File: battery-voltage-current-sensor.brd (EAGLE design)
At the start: 100 x 90 mm, 1 part

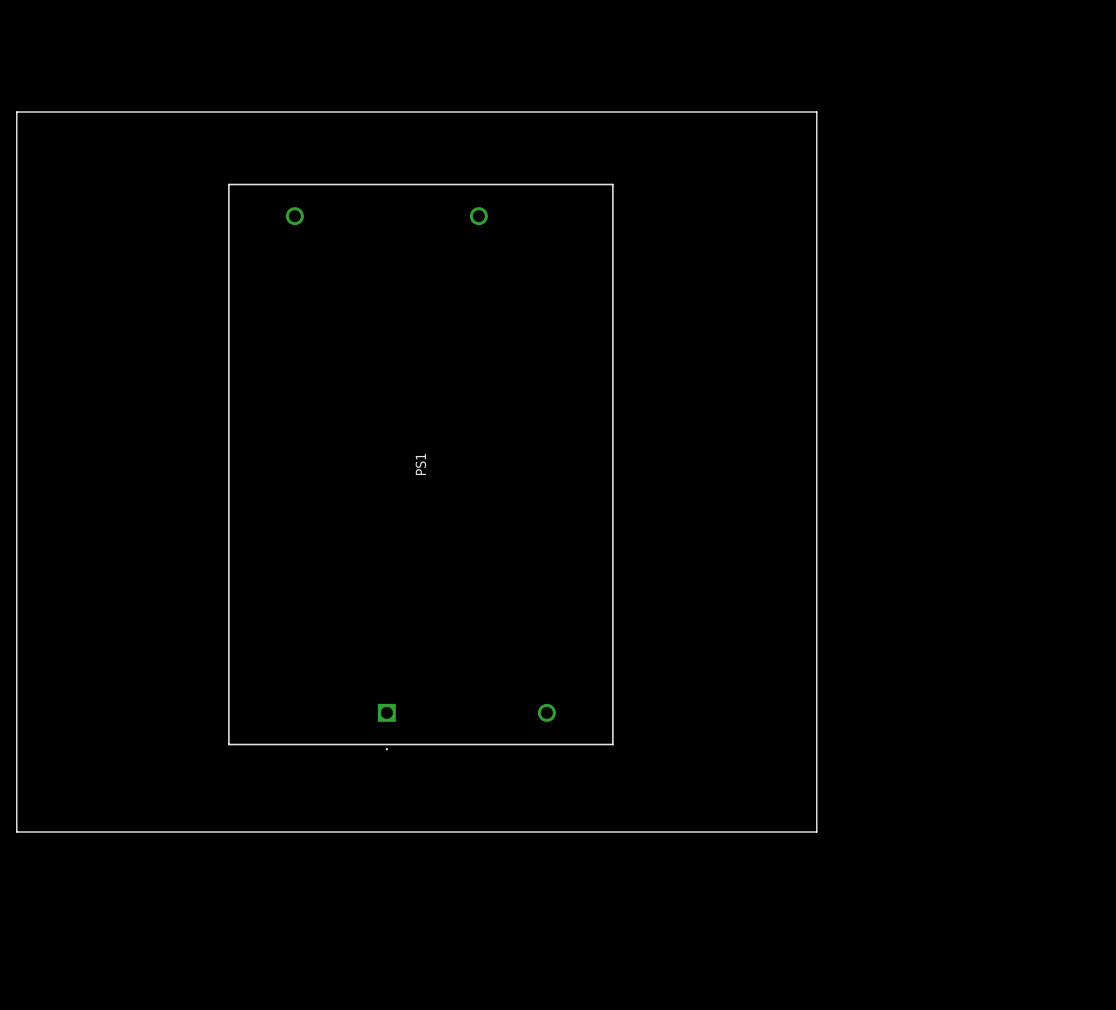
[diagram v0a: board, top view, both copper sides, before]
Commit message: basic board and holes added
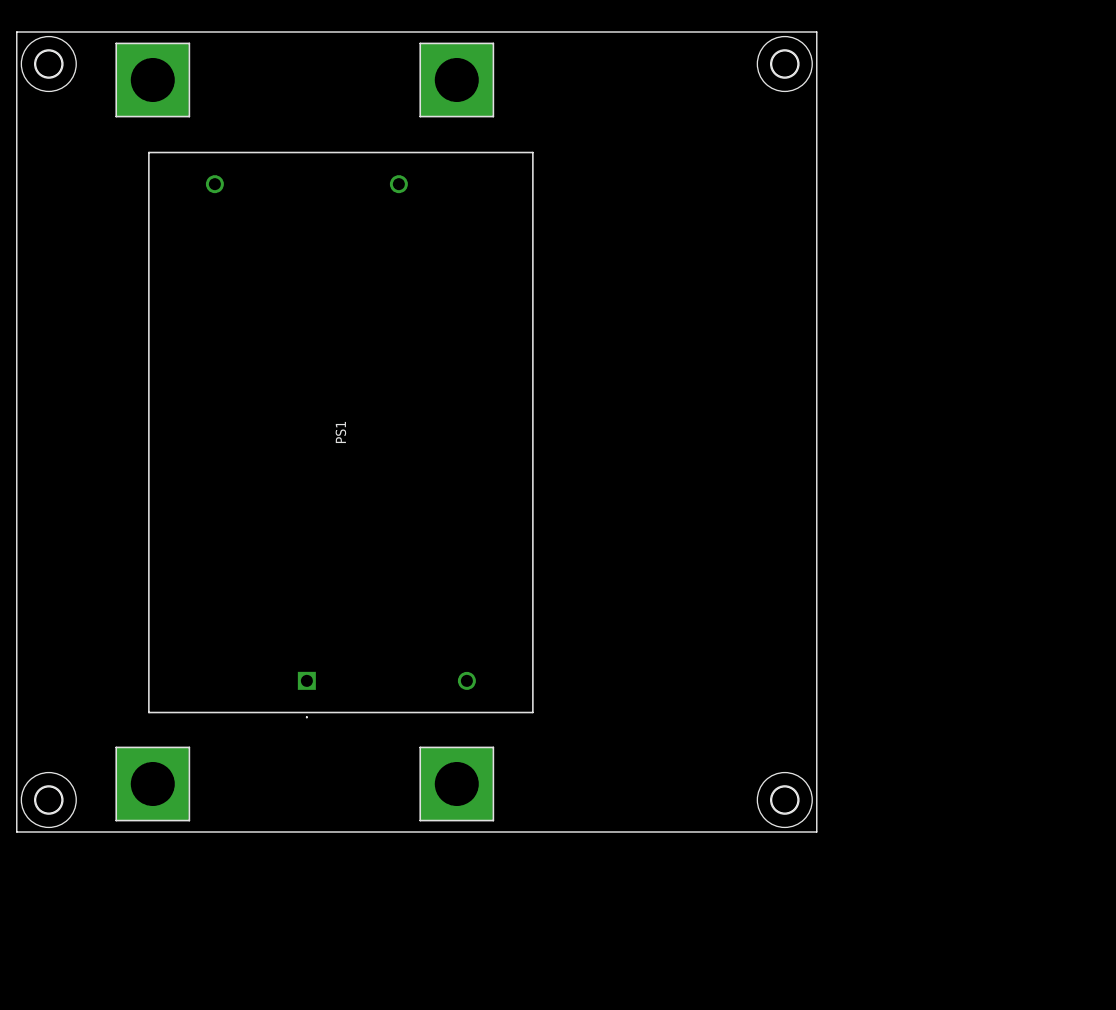
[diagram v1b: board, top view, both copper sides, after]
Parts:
- added H1, H2, H3, H4: MOUNT-PAD-SQUARE5.5, holes:5,5-PAD-SQUARE
- added H5, H6, H7, H8: MOUNT-HOLE3.3, holes:3,3
- moved PS1 10.8 mm to (36.3, 18.9)
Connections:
- new net N$1: H1.B5,5, H2.B5,5, PS1.2
- new net N$2: H3.B5,5, H4.B5,5, PS1.1
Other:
- board size 100 x 90 mm -> 100 x 100 mm
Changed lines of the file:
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@@
 <plain>
 <wire x1="0" y1="0" x2="100" y2="0" width="0" layer="20"/>
-<wire x1="100" y1="0" x2="100" y2="90" width="0" layer="20"/>
-<wire x1="100" y1="90" x2="0" y2="90" width="0" layer="20"/>
-<wire x1="0" y1="90" x2="0" y2="0" width="0" layer="20"/>
+<wire x1="100" y1="0" x2="100" y2="100" width="0" layer="20"/>
+<wire x1="100" y1="100" x2="0" y2="100" width="0" layer="20"/>
+<wire x1="0" y1="100" x2="0" y2="0" width="0" layer="20"/>
 </plain>
 <attributes>
@@
 </autorouter>
 <elements>
-<element name="PS1" library="SamacSys_Parts" package="PV1527B12R3" value="PV15-27B12R3" x="46.26" y="14.89" smashed="yes" rot="R90">
-<attribute name="DESCRIPTION" value="Isolated Module DC DC Converter 1 Output 12V 1.25A 100V - 1000V Input" x="76.74" y="94.9" size="1.778" layer="27" rot="R90" display="off"/>
-<attribute name="HEIGHT" value="24mm" x="76.74" y="94.9" size="1.778" layer="27" rot="R90" display="off"/>
-<attribute name="MANUFACTURER_NAME" value="Mornsun Power" x="76.74" y="94.9" size="1.778" layer="27" rot="R90" display="off"/>
-<attribute name="MANUFACTURER_PART_NUMBER" value="PV15-27B12R3" x="76.74" y="94.9" size="1.778" layer="27" rot="R90" display="off"/>
-<attribute name="MOUSER_PART_NUMBER" value="" x="76.74" y="94.9" size="1.778" layer="27" rot="R90" display="off"/>
-<attribute name="MOUSER_PRICE-STOCK" value="" x="76.74" y="94.9" size="1.778" layer="27" rot="R90" display="off"/>
-<attribute name="NAME" x="50.51" y="45.935" size="1.27" layer="25" rot="R90" align="center"/>
-<attribute name="VALUE" x="50.51" y="45.935" size="1.27" layer="27" rot="R90" align="center"/>
+<element name="PS1" library="SamacSys_Parts" package="PV1527B12R3" value="PV15-27B12R3" x="36.26" y="18.89" smashed="yes" rot="R90">
+<attribute name="DESCRIPTION" value="Isolated Module DC DC Converter 1 Output 12V 1.25A 100V - 1000V Input" x="66.74" y="98.9" size="1.778" layer="27" rot="R90" display="off"/>
+<attribute name="HEIGHT" value="24mm" x="66.74" y="98.9" size="1.778" layer="27" rot="R90" display="off"/>
+<attribute name="MANUFACTURER_NAME" value="Mornsun Power" x="66.74" y="98.9" size="1.778" layer="27" rot="R90" display="off"/>
+<attribute name="MANUFACTURER_PART_NUMBER" value="PV15-27B12R3" x="66.74" y="98.9" size="1.778" layer="27" rot="R90" display="off"/>
+<attribute name="MOUSER_PART_NUMBER" value="" x="66.74" y="98.9" size="1.778" layer="27" rot="R90" display="off"/>
+<attribute name="MOUSER_PRICE-STOCK" value="" x="66.74" y="98.9" size="1.778" layer="27" rot="R90" display="off"/>
+<attribute name="NAME" x="40.51" y="49.935" size="1.27" layer="25" rot="R90" align="center"/>
+<attribute name="VALUE" x="40.51" y="49.935" size="1.27" layer="27" rot="R90" align="center"/>
 </element>
+<element name="H1" library="holes" library_urn="urn:adsk.eagle:library:237" package="5,5-PAD-SQUARE" package3d_urn="urn:adsk.eagle:package:14299/1" value="MOUNT-PAD-SQUARE5.5" x="55" y="6" smashed="yes"/>
+<element name="H2" library="holes" library_urn="urn:adsk.eagle:library:237" package="5,5-PAD-SQUARE" package3d_urn="urn:adsk.eagle:package:14299/1" value="MOUNT-PAD-SQUARE5.5" x="55" y="94" smashed="yes"/>
+<element name="H3" library="holes" library_urn="urn:adsk.eagle:library:237" package="5,5-PAD-SQUARE" package3d_urn="urn:adsk.eagle:package:14299/1" value="MOUNT-PAD-SQUARE5.5" x="17" y="6" smashed="yes"/>
+<element name="H4" library="holes" library_urn="urn:adsk.eagle:library:237" package="5,5-PAD-SQUARE" package3d_urn="urn:adsk.eagle:package:14299/1" value="MOUNT-PAD-SQUARE5.5" x="17" y="94" smashed="yes"/>
+<element name="H5" library="holes" library_urn="urn:adsk.eagle:library:237" package="3,3" package3d_urn="urn:adsk.eagle:package:14278/1" value="MOUNT-HOLE3.3" x="4" y="4" smashed="yes"/>
+<element name="H6" library="holes" library_urn="urn:adsk.eagle:library:237" package="3,3" package3d_urn="urn:adsk.eagle:package:14278/1" value="MOUNT-HOLE3.3" x="4" y="96" smashed="yes"/>
+<element name="H7" library="holes" library_urn="urn:adsk.eagle:library:237" package="3,3" package3d_urn="urn:adsk.eagle:package:14278/1" value="MOUNT-HOLE3.3" x="96" y="4" smashed="yes"/>
+<element name="H8" library="holes" library_urn="urn:adsk.eagle:library:237" package="3,3" package3d_urn="urn:adsk.eagle:package:14278/1" value="MOUNT-HOLE3.3" x="96" y="96" smashed="yes"/>
 </elements>
 <signals>
+<signal name="N$1">
+<contactref element="H1" pad="B5,5"/>
+<contactref element="H2" pad="B5,5"/>
+<contactref element="PS1" pad="2"/>
+<wire x1="55" y1="6" x2="56.26" y2="18.89" width="0" layer="19" extent="1-1"/>
+<wire x1="55" y1="94" x2="55" y2="6" width="0" layer="19" extent="1-1"/>
+</signal>
+<signal name="N$2">
+<contactref element="H4" pad="B5,5"/>
+<contactref element="H3" pad="B5,5"/>
+<contactref element="PS1" pad="1"/>
+<wire x1="17" y1="6" x2="36.26" y2="18.89" width="0" layer="19" extent="1-1"/>
+<wire x1="17" y1="94" x2="17" y2="6" width="0" layer="19" extent="1-1"/>
+</signal>
 </signals>
 <mfgpreviewcolors>
@@
 </board>
 </drawing>
+<compatibility>
+<note version="8.2" severity="warning">
+Since Version 8.2, EAGLE supports online libraries. The ids
+of those online libraries will not be understood (or retained)
+with this version.
+</note>
+<note version="8.3" severity="warning">
+Since Version 8.3, EAGLE supports URNs for individual library
+assets (packages, symbols, and devices). The URNs of those assets
+will not be understood (or retained) with this version.
+</note>
+<note version="8.3" severity="warning">
+Since Version 8.3, EAGLE supports the association of 3D packages
+with devices in libraries, schematics, and board files. Those 3D
+packages will not be understood (or retained) with this version.
+</note>
+</compatibility>
 </eagle>

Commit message: mounting holes added
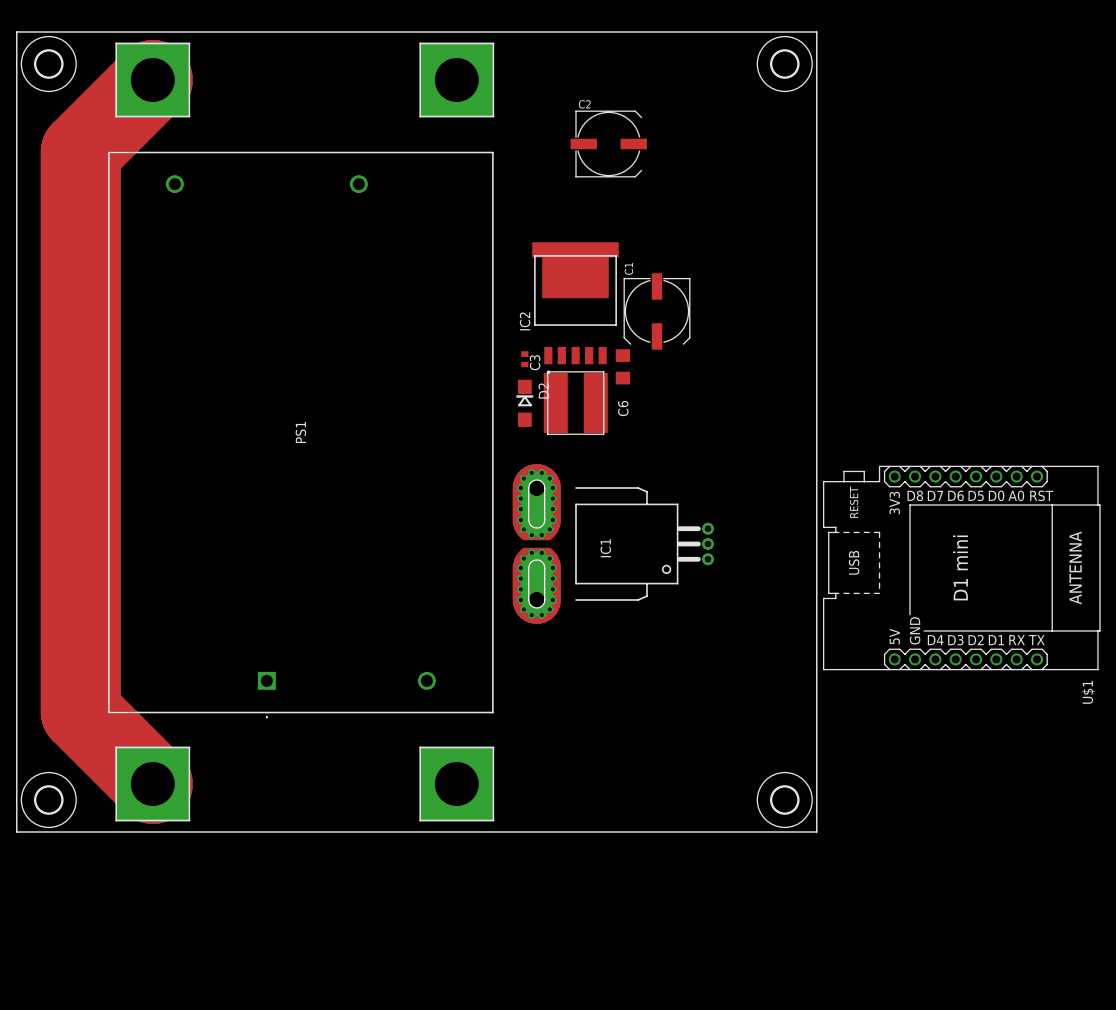
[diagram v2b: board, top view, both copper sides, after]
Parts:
- added C1, C2: C249880, rcl:UD-8X10_NICHICON
- added C3: 100n, rcl:C0402
- added C6: 1uF, rcl:C1206
- added D2: C16015, diode:DO214AC
- added IC1: ACS758LCB-050B-PFF-T, allegro:CB-PFF
- added IC2: LM2596S-5.0_NOPB, SamacSys_Parts:KTT0005B
- added L2: C2929443, SamacSys_Parts:CY75-100UH
- added U$1: WEMOS-D1-MINI, diy-modules:WEMOS-D1-MINI
- moved PS1 5.00 mm to (31.3, 18.9)
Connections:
- new net +5V/1: C1.+, C6.1, IC2.4, L2.P$2
- new net 3V3: U$1.JP1.8
- new net 5V: U$1.JP2.8
- new net C12+: C2.+, C3.1, IC2.1
- new net GND: C1.-, C2.-, C3.2, C6.2, D2.A, IC1.2, IC2.3, IC2.5, IC2.6, IC2.7, IC2.8, U$1.JP2.7
- new net N$3: D2.C, IC2.2, L2.P$1
- new net VCC: IC1.1
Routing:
- net N$2: track 0.00 -> 190.9 mm

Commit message: first placing check
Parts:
- moved IC1 40.3 mm to (55.0, 75.0)
- moved PS1 34.1 mm to (6.89, 42.7), turned to 0 degrees
- moved U$1 31.8 mm to (87.0, 26.0), turned to 0 degrees
- moved C1 15.1 mm to (95.0, 63.1)
- moved C2 15.1 mm to (89.0, 84.0)
- moved C3 15.1 mm to (78.5, 57.1)
- moved C6 15.1 mm to (90.8, 56.1)
- moved D2 15.1 mm to (78.5, 51.6)
- moved IC2 15.1 mm to (84.8, 63.7)
- moved L2 15.1 mm to (84.9, 51.6)
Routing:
- net N$2: track 190.9 -> 0.00 mm

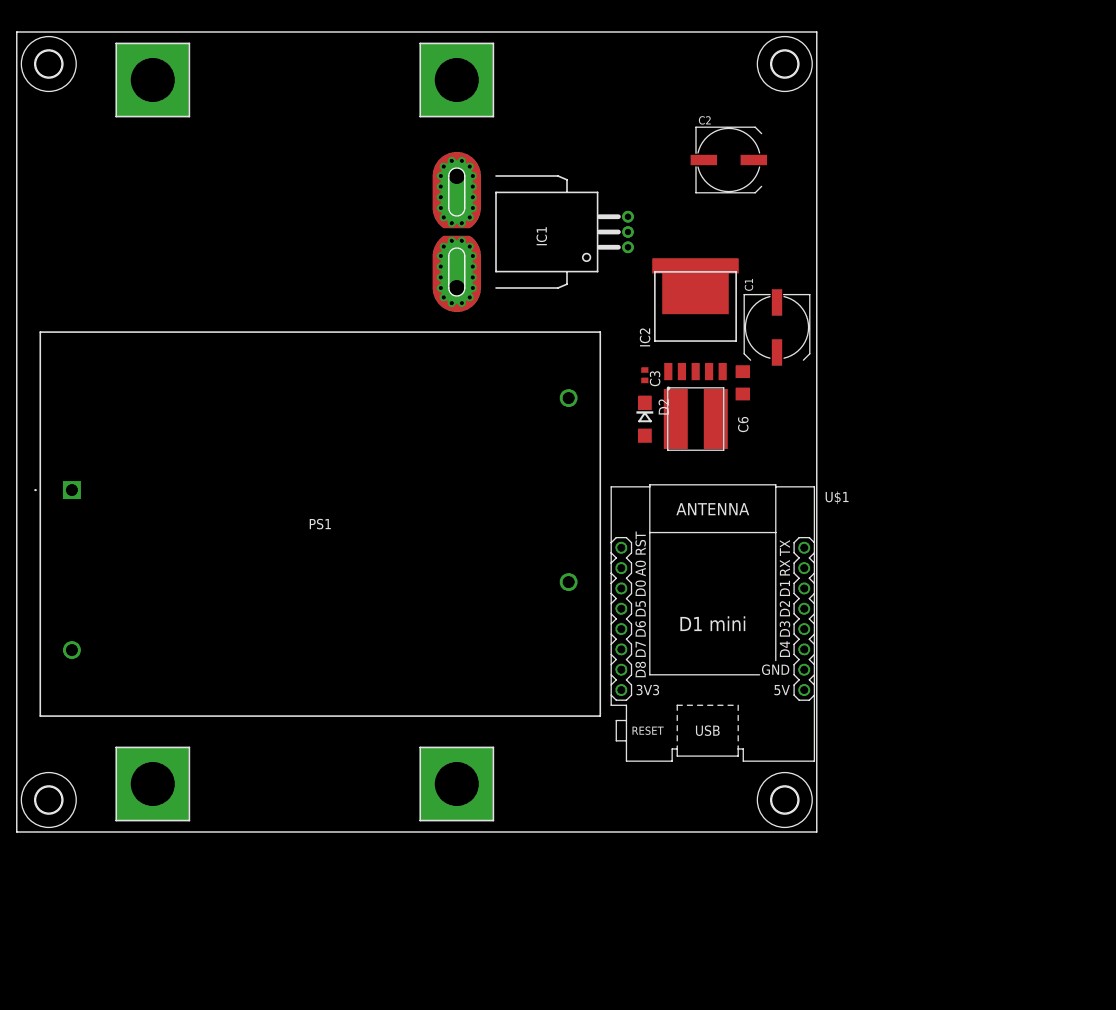
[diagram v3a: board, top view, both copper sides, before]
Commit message: DCDC as a module added
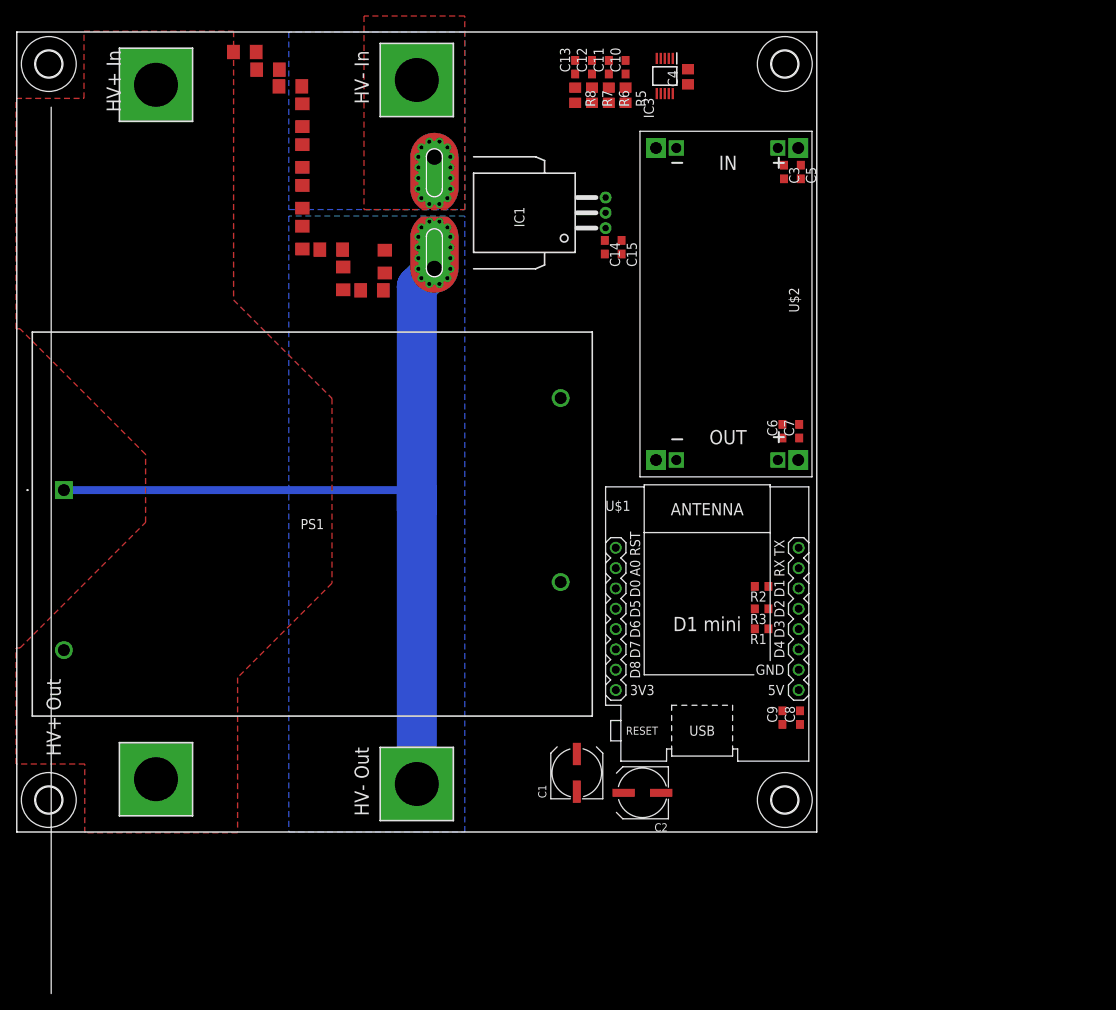
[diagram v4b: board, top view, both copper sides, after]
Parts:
- removed D2: C16015, diode:DO214AC
- removed IC2: LM2596S-5.0_NOPB, SamacSys_Parts:KTT0005B
- removed L2: C2929443, SamacSys_Parts:CY75-100UH
- added C10, C11, C12, C13, C14, C15, C5, C7, C8, C9: 100nF, rcl:C0603
- added C4: 100nF, rcl:C0805
- added IC3: ADS1115IDGST, SamacSys_Parts:SOP50P490X110-10N
- added R1, R2, R3: 10k, rcl:R0603
- added R15, R16, R17, R18, R19, R20, R21, R22, R23, R4: 120k, rcl:R1206
- added R24: 10k 1206, rcl:R1206
- added R5, R6, R7, R8: 1k, rcl:R0805
- added U$2: DC-DC-STEP-DOWN-LM2596HVS, diy-modules:DC-DC-STEP-DOWN-LM2596HVS
- C1: value C249880 -> C473426; device rcl:UD-8X10_NICHICON -> rcl:UD-6,3X7,7_NICHICON
- C2: value C249880 -> (none); device rcl:UD-8X10_NICHICON -> rcl:UD-6,3X7,7_NICHICON
- C3: value 100n -> 100nF; device rcl:C0402 -> rcl:C0603
- C6: value 1uF -> 100nF; device rcl:C1206 -> rcl:C0603
- moved H3 94.0 mm to (50.0, 94.0)
- moved H4 94.0 mm to (50.0, 6.00)
- moved C2 79.8 mm to (78.2, 4.90), turned to 180 degrees
- moved C1 61.0 mm to (70.0, 7.40), turned to 90 degrees
- moved H1 37.6 mm to (17.4, 6.60)
- moved H2 37.6 mm to (17.4, 93.4)
- moved C3 30.8 mm to (95.9, 82.5)
- moved C6 7.81 mm to (95.7, 50.1)
- moved IC1 3.69 mm to (52.2, 77.4)
- moved PS1 1.00 mm to (5.89, 42.7)
- moved U$1 0.70 mm to (86.3, 26.0)
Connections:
- removed net 3V3: U$1.JP1.8
- removed net 5V: U$1.JP2.8
- removed net C12+: C2.+, C3.1, IC2.1
- removed net N$2: H3.B5,5, H4.B5,5, PS1.1
- removed net VCC: IC1.1
- new net +12V/1: C1.+, C3.1, C5.1, PS1.3, U$2.IN+
- new net +3.3V/1: R1.2, R2.2, R3.2, U$1.JP1.8
- new net AIN0: C13.1, IC3.4, R8.1
- new net AIN1: C12.1, IC3.5, R7.1
- new net AIN2: C11.1, IC3.6, R6.1
- new net AIN3: C10.1, IC3.7, R5.1
- new net HV+: H1.B5,5, H2.B5,5, PS1.2, R23.2
- new net HV-: H4.B5,5, IC1.IP-, IC1.IP-@10, IC1.IP-@11, IC1.IP-@12, IC1.IP-@13, IC1.IP-@14, IC1.IP-@15, IC1.IP-@16, IC1.IP-@17, IC1.IP-@2, IC1.IP-@3, IC1.IP-@4, IC1.IP-@5, IC1.IP-@6, IC1.IP-@7, IC1.IP-@8, IC1.IP-@9, PS1.1, R24.1
- new net HV-IN: H3.B5,5, IC1.IP+, IC1.IP+@10, IC1.IP+@11, IC1.IP+@12, IC1.IP+@13, IC1.IP+@14, IC1.IP+@15, IC1.IP+@16, IC1.IP+@17, IC1.IP+@2, IC1.IP+@3, IC1.IP+@4, IC1.IP+@5, IC1.IP+@6, IC1.IP+@7, IC1.IP+@8, IC1.IP+@9
- new net N$10: R16.2, R17.1
- new net N$11: R17.2, R18.1
- new net N$12: R18.2, R19.1
- new net N$13: R19.2, R20.1
- new net N$14: R20.2, R21.1
- new net N$15: R21.2, R22.1
- new net N$16: R22.2, R23.1
- new net N$18: R7.2
- new net N$4: IC3.10, R2.1, U$1.JP2.3
- new net N$5: IC3.9, R3.1, U$1.JP2.4
- new net N$7: R6.2
- new net N$8: R15.1, R4.2
- new net N$9: R15.2, R16.1
- new net SIGNALHV: R24.2, R4.1
- new net VOUTCURRENT: IC1.3, R8.2
- net +5V/1: now also C14.1, C15.1, C2.+, C4.1, C7.1, C8.2, C9.2, IC1.1, IC3.8, U$1.JP2.8, U$2.OUT+; no longer C1.+, IC2.4, L2.P$2
- net GND: now also C10.2, C11.2, C12.2, C13.2, C14.2, C15.2, C4.2, C5.2, C7.2, C8.1, C9.1, IC3.1, IC3.3, PS1.4, U$2.IN-, U$2.OUT-; no longer D2.A, IC2.3, IC2.5, IC2.6, IC2.7, IC2.8
- net N$1: now also IC3.2, R1.1, U$1.JP2.5; no longer H1.B5,5, H2.B5,5, PS1.2
- net N$3: now also R5.2; no longer D2.C, IC2.2, L2.P$1
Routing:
- net HV-: track 0.00 -> 111.9 mm
- added copper zone on layer 1, net HV+
- added copper zone on layer 16, net HV-
- added copper zone on layer 1, net HV-IN
- added copper zone on layer 16, net HV-IN
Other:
- board text added: "HV+ In"
- board text added: "HV+ Out"
- board text added: "HV- In"
- board text added: "HV- Out"
